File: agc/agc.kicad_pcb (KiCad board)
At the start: 4 copper layers, 72.4 x 99.8 mm, 110 parts, among them J1 SMA_DAC, J2 SMA_LPTR, J3 SMA_DRIVER, J4 SMA_RX, J5 SIL10, J6 SMA_LPTR, K1 TR, K3 VIN, K5 TR, K7 HVMON, P10 CONN_2, P2 FWD_FAULT, P3 REF_FAULT, P4 CONN_8X2, P5 COUPLED_TEST, P6 TP_VCC, P7 COUPLED_TEST, P8 COUPLED_TEST, P9 COUPLED_TEST, U1 BA08CC0WFP, U10 74AHC1G04, U11 74AHC1G04, U12 78SRH-5/2-C, U14 SMP1330-005LF, U15 SMP1330-005LF, U16 SMP1330-005LF, U2 HMC475, U3 HMC595, U4 HMC595, U5 HMC595, U6 74AHC1G04, U7 ISL3281E, U8 MGA-61563, U9 LTC2914-2

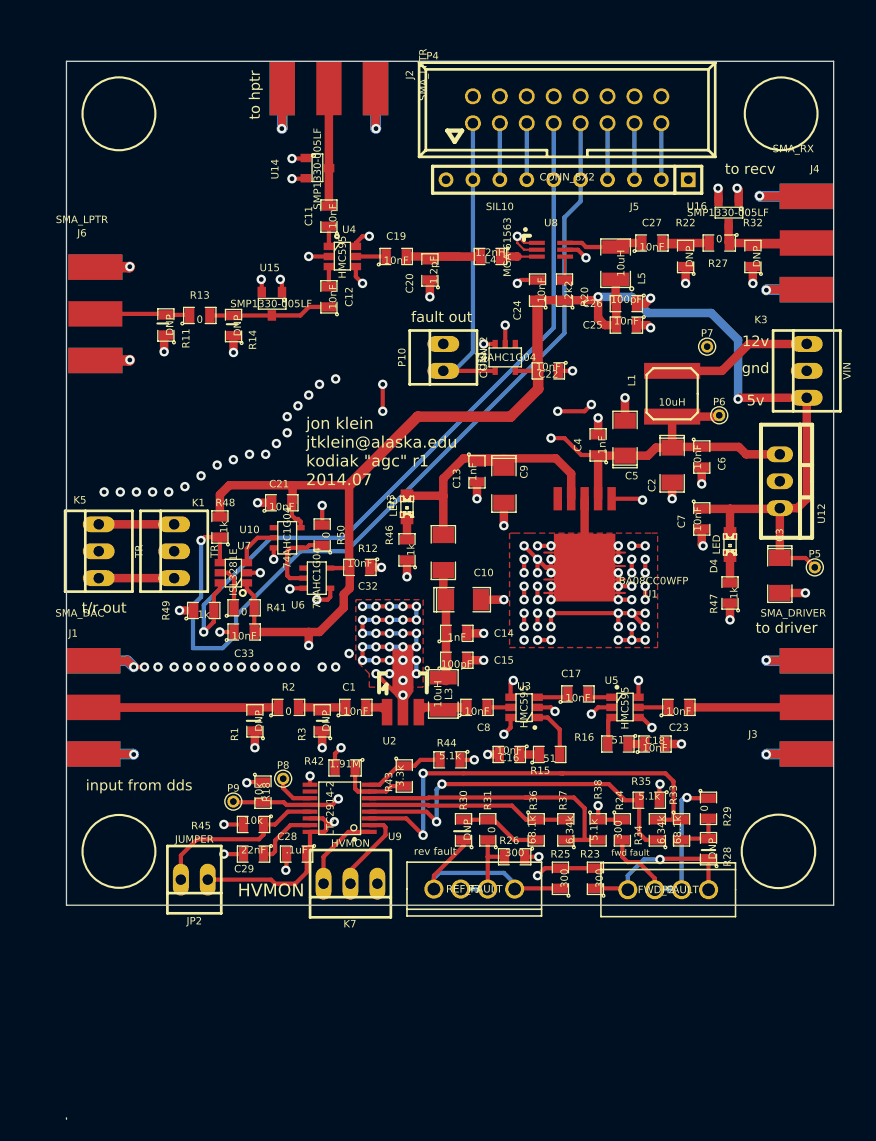
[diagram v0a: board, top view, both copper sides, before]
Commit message: polishing agc, tr, and driver amp for next revisions. moved all bottom layer signal traces to top layer on driver amp
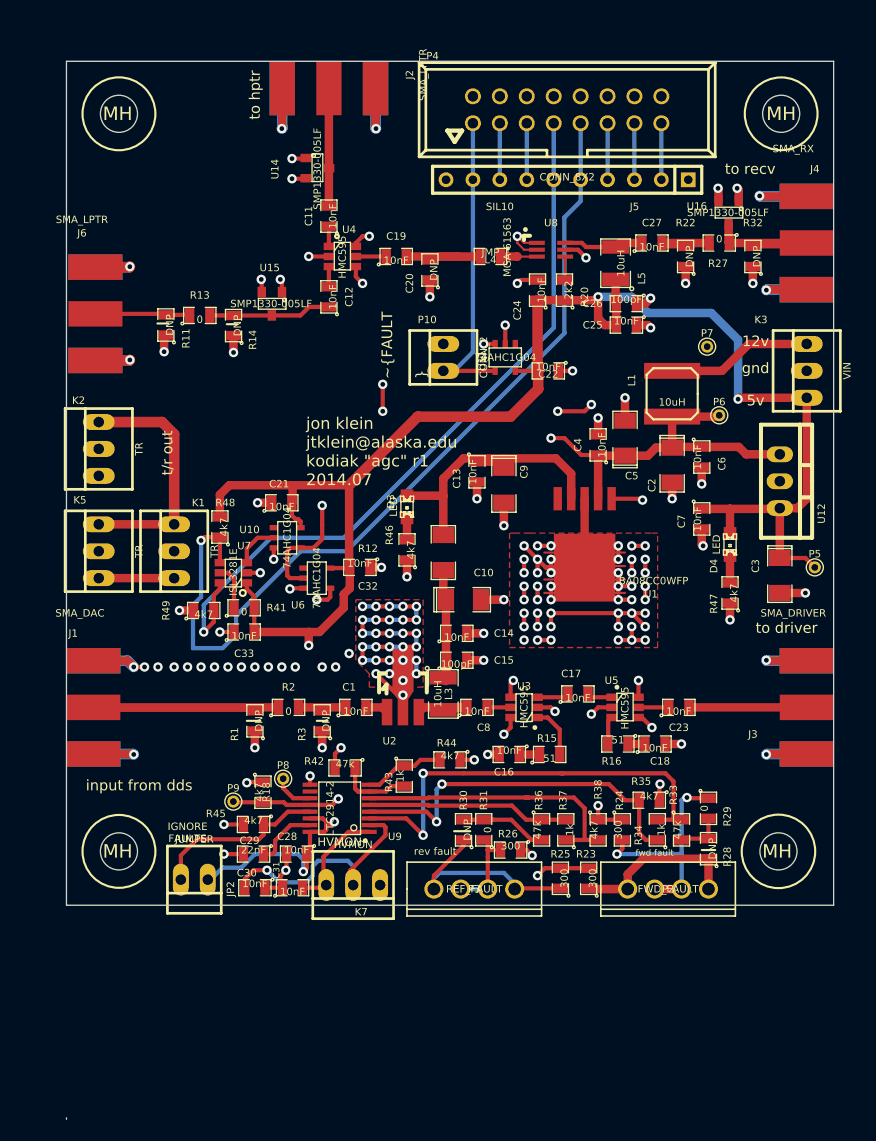
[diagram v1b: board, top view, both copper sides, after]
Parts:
- removed R50: 0, SMD_Packages:SM0805
- added C30: 10nF, SMD_Packages:SM0805, F.Cu at (50.8, 111.0)
- added C31: 10nF, SMD_Packages:SM0805, F.Cu at (54.4, 111.0)
- added K2: TR, Connect:PINHEAD1-3, F.Cu at (36.1, 69.6)
- added MH: MountingHole_3-5mm_RevA_Date21Jun2010, Mounting_Holes:MountingHole_3-5mm, F.Cu at (38.0, 38.0)
- added MH: MountingHole_3-5mm_RevA_Date21Jun2010, Mounting_Holes:MountingHole_3-5mm, F.Cu at (38.0, 107.6)
- added MH: MountingHole_3-5mm_RevA_Date21Jun2010, Mounting_Holes:MountingHole_3-5mm, F.Cu at (100.2, 107.6)
- added MH: MountingHole_3-5mm_RevA_Date21Jun2010, Mounting_Holes:MountingHole_3-5mm, F.Cu at (100.5, 38.0)
- C13, C14, C4: value 1nF -> 10nF
- C20: value 1.2pF -> DNP
- C28: value .1uF -> 10nF
- L4: value 1.2nH -> JMP
- R18, R45: value 10k -> 4k7
- R33, R36: value 68.1k -> 47k
- R34, R37: value 6.34k -> 1k
- R35, R38, R44: value 5.1k -> 4k7
- R42: value 1.91M -> 47k
- R43: value 3.3k -> 1k
- R46, R47, R48, R49: value 1k -> 4k7
- moved R26 0.74 mm to (74.9, 107.4)
- moved R23 0.63 mm to (82.3, 110.1)
- moved R36 0.51 mm to (77.9, 105.5)
- moved R31 0.38 mm to (72.4, 105.5)
- moved K7 0.28 mm to (60.1, 110.7)
- moved P2 0.06 mm to (89.8, 111.1), turned to 0 degrees
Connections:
- U10 pad 4: Net-(R50-Pad1) -> /~TX
- U6 pad 2: Net-(R50-Pad1) -> /~TX
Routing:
- net (no net): track 32.9 -> 0.00 mm, vias 18 -> 0
- net /~TX: track 168.1 -> 193.3 mm
- net Net-(C30-Pad2): track 8.81 -> 24.0 mm, vias 0 -> 1
- net /TX: track 121.7 -> 136.0 mm
- net GND: track 325.7 -> 335.9 mm
- net Net-(R50-Pad1): track 7.45 -> 0.00 mm
- net Net-(C31-Pad2): track 8.35 -> 10.7 mm
- net +5V: track 226.5 -> 228.0 mm, vias 6 -> 7
- net Net-(P2-Pad2): track 20.1 -> 21.2 mm, vias 1 -> 2
- net Net-(R30-Pad2): track 7.65 -> 8.73 mm
- net Net-(P2-Pad1): track 16.0 -> 15.6 mm, vias 1 -> 0
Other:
- board text added: "IGNORE FAULTS"
- board text added: "~FAULT"
- board text removed: "fault out"

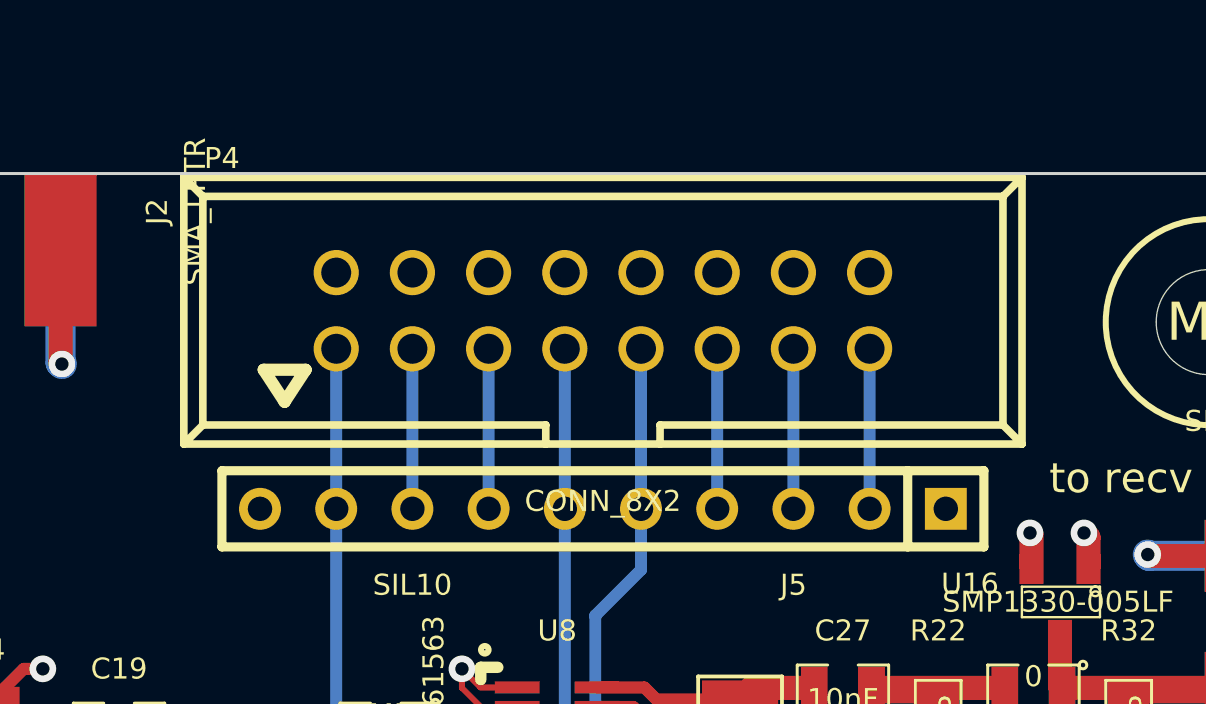
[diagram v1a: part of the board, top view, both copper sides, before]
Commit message: fixed footprint
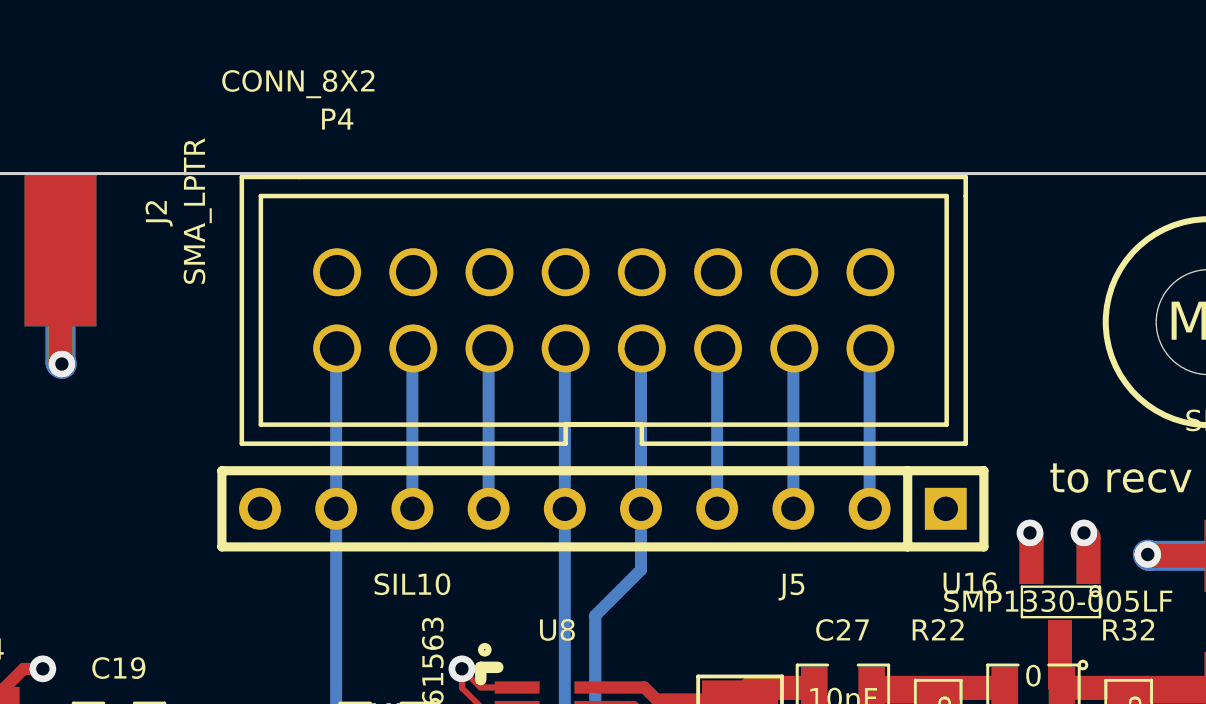
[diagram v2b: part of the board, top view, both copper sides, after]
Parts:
- P4: footprint Connect:VASCH8x2 -> ocal:conn_8x2

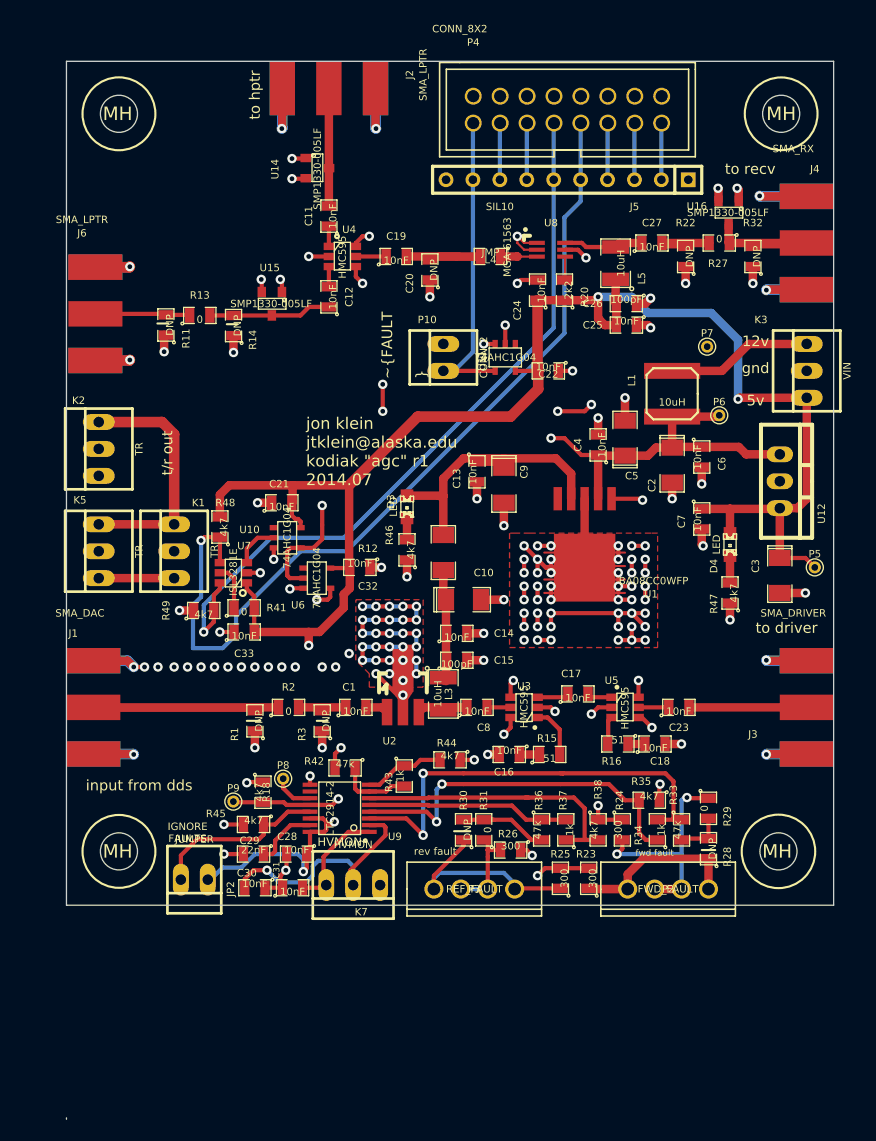
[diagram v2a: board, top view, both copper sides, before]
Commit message: added extra power header to control board, added spam to driver amp bottom soldermask layer to pass oshpark check script, added board outlines to agc and tr silkscreen
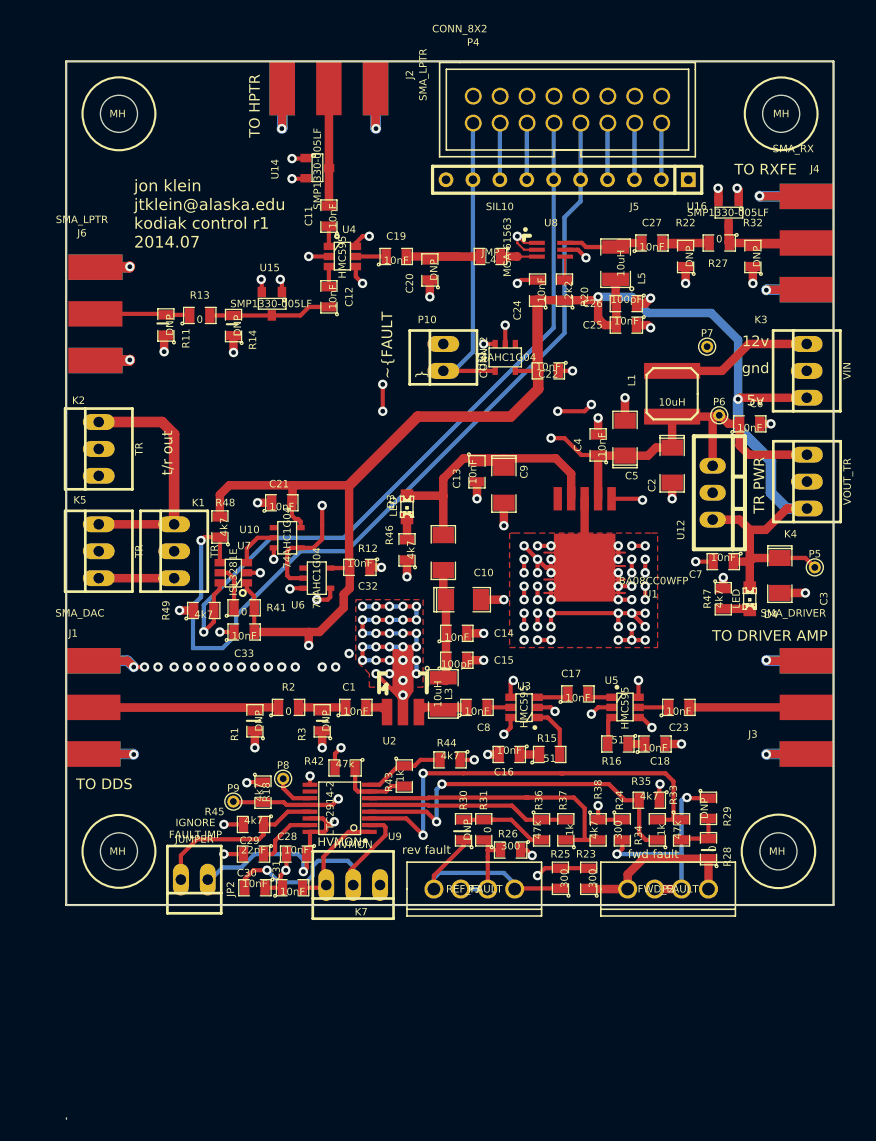
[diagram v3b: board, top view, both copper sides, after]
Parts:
- added K4: VOUT_TR, Connect:PINHEAD1-3, F.Cu at (102.9, 72.7)
- R28: value DNP -> 0
- R29: value 0 -> DNP
- moved U12 6.43 mm to (94.0, 73.7)
- moved C6 5.50 mm to (97.5, 67.2), turned to 0 degrees
- moved D4 5.45 mm to (97.5, 83.7)
- moved C7 4.51 mm to (95.0, 80.2), turned to 180 degrees
- moved R47 0.84 mm to (95.0, 83.7), turned to 270 degrees
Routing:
- net +5V: track 228.0 -> 235.4 mm
- net VCC: track 79.3 -> 85.0 mm
- net GND: track 335.9 -> 334.9 mm
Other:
- board text added: "IGNORE FAULT JMP"
- board text added: "TO DDS"
- board text added: "TO DRIVER AMP"
- board text added: "TO HPTR"
- board text added: "TO RXFE"
- board text added: "TR PWR"
- board text added: "jon klein jtklein@alaska.edu kodiak control r1 2014.07"
- board text removed: "IGNORE FAULTS"
- board text removed: "input from dds"
- board text removed: "jon klein jtklein@alaska.edu kodiak "agc" r1 2014.07"
- board text removed: "to driver"
- board text removed: "to hptr"
- board text removed: "to recv"

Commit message: switched to through hole SMA connectors on rxfe and control board, added larger mounting holes for rxfe to mount directly to shelf
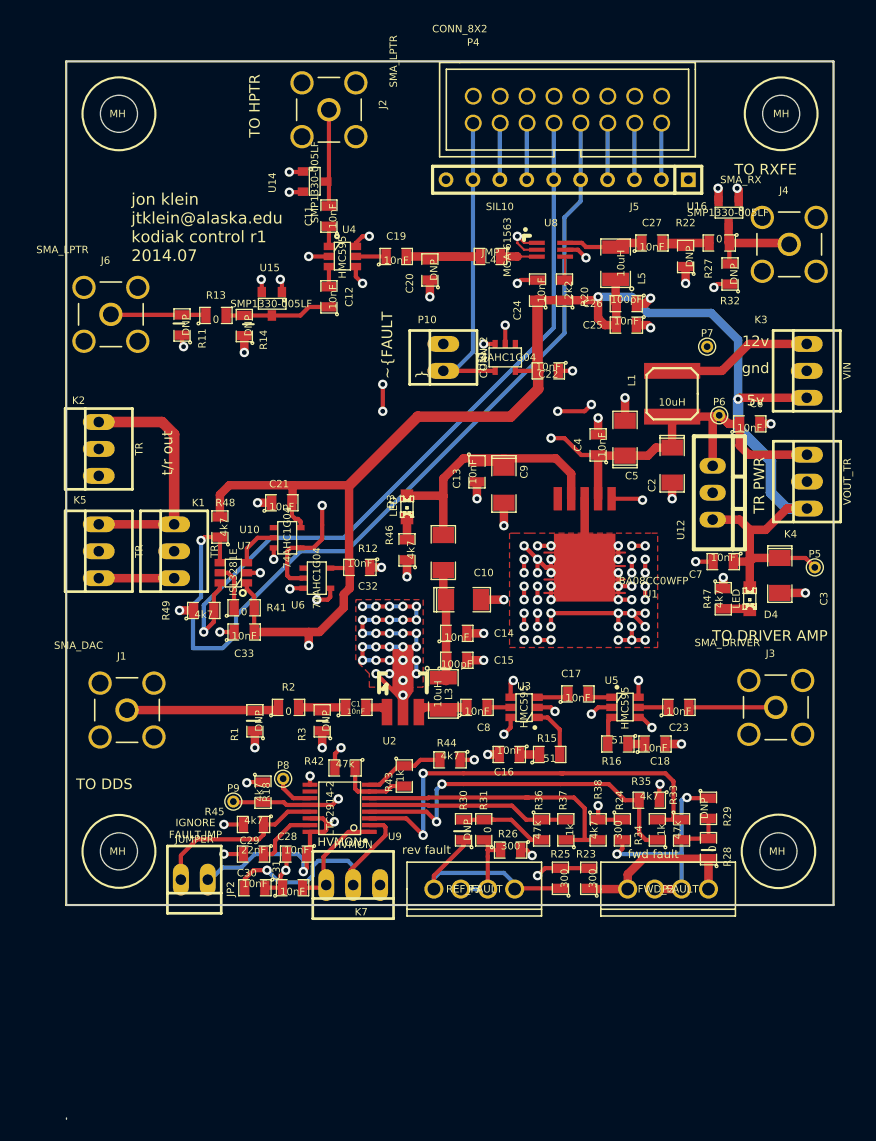
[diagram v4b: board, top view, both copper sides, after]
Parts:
- C1: footprint SMD_Packages:SM0805 -> SMD_Packages:SMD-0805
- J1, J2, J3, J4, J6: footprint sma:sma -> ocal:SMA_5-1814832-1
- moved J1 3.19 mm to (38.7, 94.2)
- moved J3 2.92 mm to (99.9, 94.0)
- moved R32 2.72 mm to (95.6, 53.1)
- moved J2 2.03 mm to (57.8, 37.6)
- moved J4 1.66 mm to (101.2, 50.3)
- moved R11 1.52 mm to (43.9, 57.9)
- moved R13 1.52 mm to (47.1, 57.0)
- moved J6 1.46 mm to (37.2, 56.9)
- moved U14 1.30 mm to (56.4, 44.4)
- moved R14 1.02 mm to (49.8, 58.0)
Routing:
- net GND: track 334.9 -> 237.4 mm, vias 156 -> 131
- net Net-(J1-Pad1): track 35.5 -> 15.2 mm
- net Net-(J4-Pad1): track 17.1 -> 9.49 mm
- net Net-(C11-Pad2): track 14.6 -> 9.33 mm
- net Net-(C23-Pad2): track 11.1 -> 8.19 mm
- net Net-(C12-Pad1): track 11.6 -> 10.6 mm

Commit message: moved amp from control board to rxfe
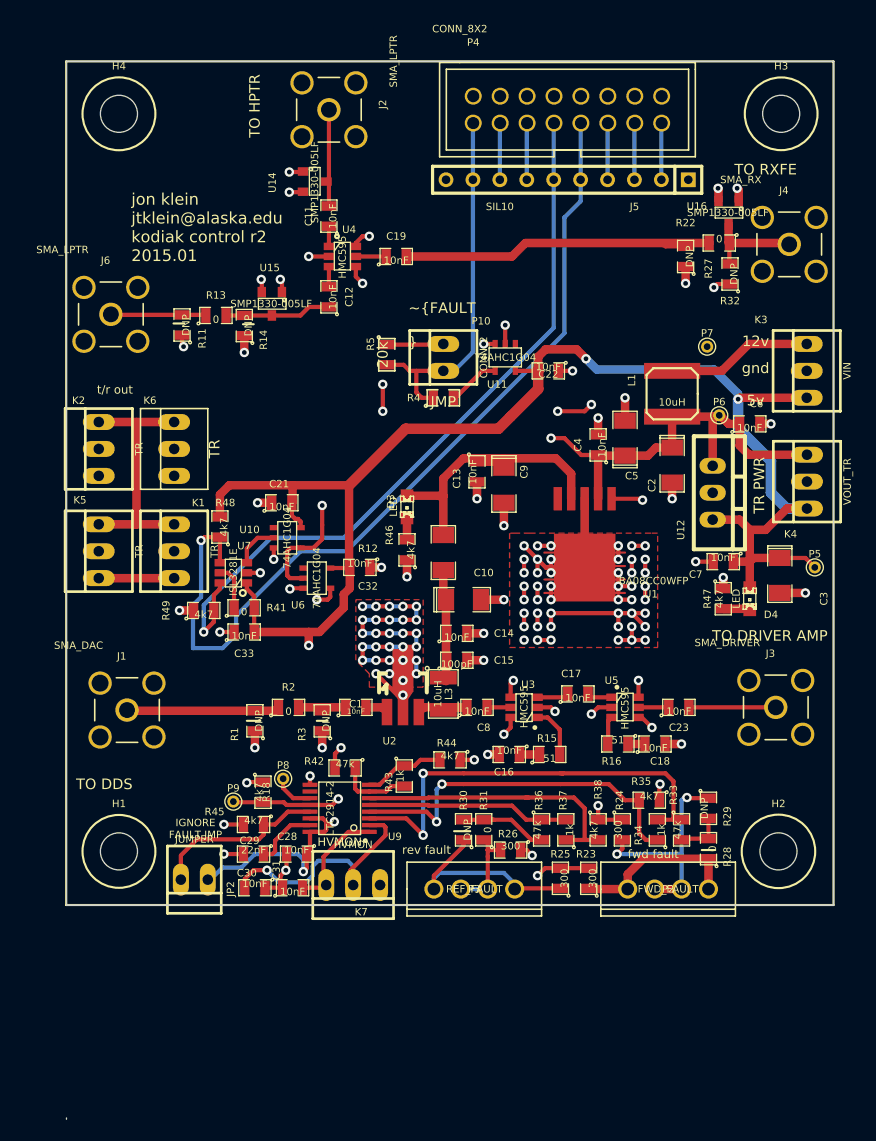
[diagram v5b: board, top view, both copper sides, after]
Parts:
- removed C20: DNP, SMD_Packages:SM0805
- removed C24, C25, C27: 10nF, SMD_Packages:SM0805
- removed C26: 100pF, SMD_Packages:SM0805
- removed L4: JMP, SMD_Packages:SM0805
- removed L5: 10uH, SMD_Packages:SM1210
- removed MH (x4): MountingHole_3-5mm_RevA_Date21Jun2010, Mounting_Holes:MountingHole_3-5mm
- removed R20: 2k2, SMD_Packages:SM0805
- removed U8: MGA-61563, Housings_SOT-23_SOT-143_TSOT-6:SC70-6_Handsoldering
- added H1: MOUNTING_HOLE, Mounting_Holes:MountingHole_3-5mm, F.Cu at (38.0, 107.6)
- added H2: MOUNTING_HOLE, Mounting_Holes:MountingHole_3-5mm, F.Cu at (100.2, 107.6)
- added H3: MOUNTING_HOLE, Mounting_Holes:MountingHole_3-5mm, F.Cu at (100.5, 38.0)
- added H4: MOUNTING_HOLE, Mounting_Holes:MountingHole_3-5mm, F.Cu at (38.0, 38.0)
- added K6: TR, Connect:PINHEAD1-3, F.Cu at (43.2, 69.6)
- added R4: JMP, SMD_Packages:SMD-0805, F.Cu at (68.6, 64.8)
- added R5: 20k, SMD_Packages:SMD-0805, F.Cu at (63.2, 60.7)
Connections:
- K3 pad 1: +5V -> (no net)
- R22 pad 2: Net-(C27-Pad2) -> Net-(C19-Pad2)
- R27 pad 2: Net-(C27-Pad2) -> Net-(C19-Pad2)
- U11 pad 4: /~FAULT -> Net-(R4-Pad2)
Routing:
- net +5V: track 235.4 -> 216.9 mm
- net Net-(C19-Pad2): track 17.2 -> 33.8 mm
- net Net-(C27-Pad2): track 9.15 -> 0.00 mm
- net GND: track 237.4 -> 229.1 mm, vias 131 -> 125
- net Net-(C27-Pad1): track 7.56 -> 0.00 mm
- net /TX: track 136.0 -> 142.1 mm
- net /~FAULT: track 30.0 -> 35.1 mm
- net Net-(R4-Pad2): track 0.00 -> 4.99 mm
- net Net-(L4-Pad1): track 3.46 -> 0.00 mm
- net Net-(R20-Pad2): track 2.23 -> 0.00 mm
- net /~TX: track 193.3 -> 194.2 mm
- net Net-(J1-Pad1): track 15.2 -> 15.7 mm
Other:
- board text added: "jon klein jtklein@alaska.edu kodiak control r2 2015.01"
- board text removed: "jon klein jtklein@alaska.edu kodiak control r1 2014.07"
